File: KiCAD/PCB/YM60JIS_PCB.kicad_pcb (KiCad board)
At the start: 2 copper layers, 285.1 x 94.6 mm, 173 parts, among them J1 TYPE-C-31-M-12, SW1 SW_Push, SW10 SW_Push, SW11 SW_Push, SW12 SW_Push, SW13 SW_Push, SW14 SW_Push, SW15 SW_Push, SW16 SW_Push, SW17 SW_Push, SW18 SW_Push, SW19 SW_Push, SW2 SW_Push, SW20 SW_Push, SW21 SW_Push, SW22 SW_Push, SW23 SW_Push, SW24 SW_Push, SW25 SW_Push, SW26 SW_Push, SW27 SW_Push, SW28 SW_Push, SW29 Space, SW3 SW_Push, SW30 SW_Push, SW31 SW_Push, SW32 SW_Push, SW33 SW_Push, SW34 SW_Push, SW35 SW_Push, SW36 SW_Push, SW37 SW_Push, SW38 SW_Push, SW39 SW_Push, SW4 SW_Push, SW40 SW_Push, SW41 SW_Push, SW42 SW_Push, SW43 SW_Push, SW44 SW_Push, SW45 SW_Push, SW46 SW_Push, SW47 SW_Push, SW48 SW_Push, SW49 SW_Push, SW5 SW_Push, SW50 SW_Push, SW51 SW_Push, SW52 SW_Push, SW53 SW_Push, SW54 SW_Push, SW55 SW_Push, SW56 SW_Push, SW57 SW_Push, SW58 SW_Push, SW59 SW_Push, SW6 SW_Push, SW60 SW_Push, SW61 SW_Push, SW62 SW_Push, SW63 Yen, SW64 Backspace, SW65 ISOEnter, SW66 SW_Push, SW67 SW_Push, SW7 SW_Push, SW8 SW_Push, SW9 SW_Push, U1 XC6206P332MR, U2 SMF05CT1G, U3 RP2040, U4 W25Q16JVUXIQ, Y1 X322512MSB4SI

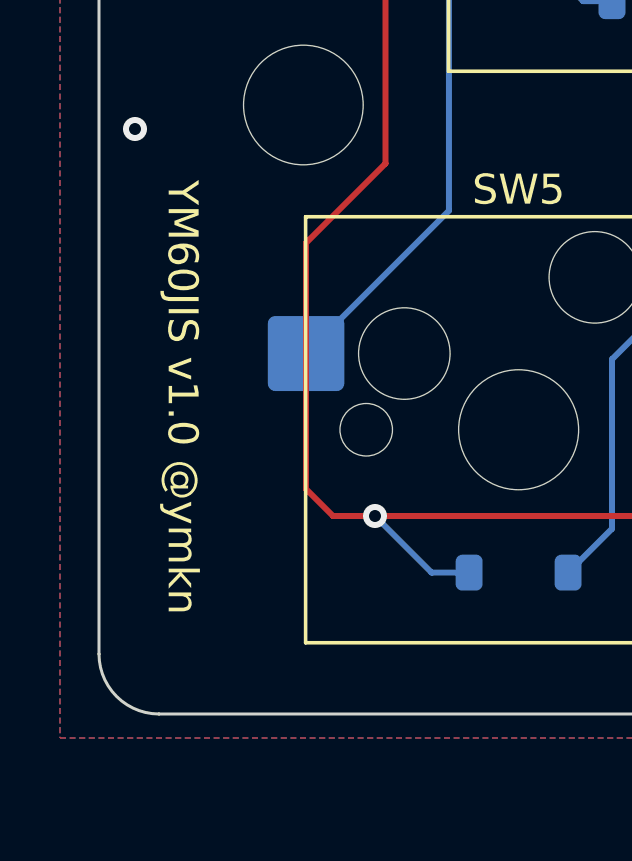
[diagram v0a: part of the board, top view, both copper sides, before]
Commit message: PlateのライブラリパスをPCBと同様にsubmoduleへ変更、穴位置も微調整
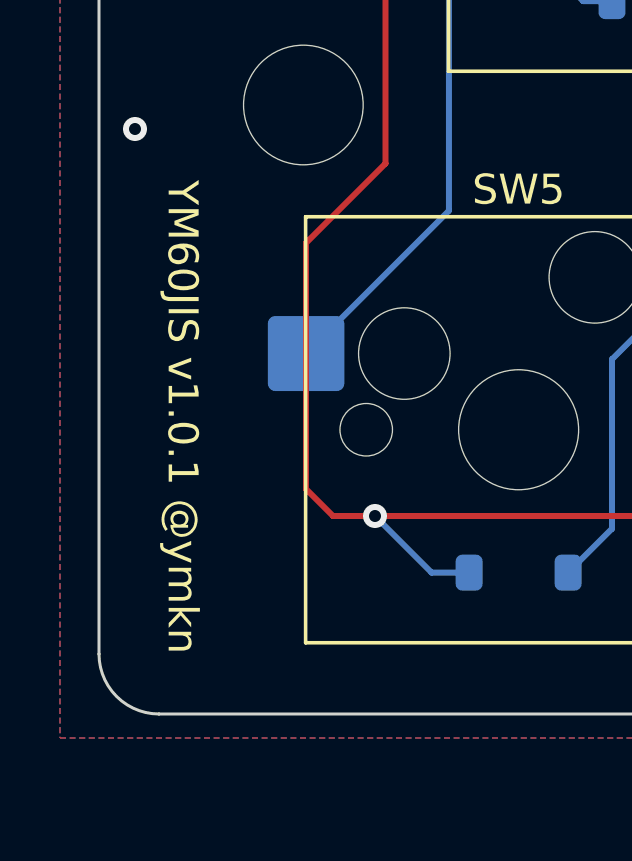
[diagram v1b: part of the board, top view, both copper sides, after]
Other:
- board text added: "YM60JIS v1.0.1 @ymkn"
- board text removed: "YM60JIS v1.0 @ymkn"
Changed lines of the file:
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@@
   (title_block
     (title "YM60JIS PCB")
-    (date "2023-11-11")
-    (rev "v1.0")
+    (date "2024-01-08")
+    (rev "v1.0.1")
     (company "@ymkn")
   )
@@
     (effects (font (size 1 1) (thickness 0.15)) (justify left bottom mirror))
   )
-  (gr_text "YM60JIS v1.0 @ymkn" (at 97.75 125.025 270) (layer "F.SilkS")
+  (gr_text "YM60JIS v1.0.1 @ymkn" (at 97.75 125.025 270) (layer "F.SilkS")
     (effects (font (size 1 1) (thickness 0.15)) (justify left bottom))
   )

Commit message: v1.1およびv1.1.1の追加
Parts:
- REF**: value Stabilizer_Cherry_MX_2.00u -> STAB_MX_ISO; footprint PCM_Mounting_Keyboard_Stabilizer:Stabilizer_Cherry_MX_2.00u -> PCM_marbastlib-mx:STAB_MX_ISO
- REF**: value Stabilizer_Cherry_MX_3.00u -> STAB_MX_2.75u; footprint PCM_Mounting_Keyboard_Stabilizer:Stabilizer_Cherry_MX_3.00u -> PCM_marbastlib-mx:STAB_MX_2.75u
- REF**: value Stabilizer_Cherry_MX_2.00u -> STAB_MX_2u; footprint PCM_Mounting_Keyboard_Stabilizer:Stabilizer_Cherry_MX_2.00u -> PCM_marbastlib-mx:STAB_MX_2u
- REF**: value Stabilizer_Cherry_MX_2.00u -> STAB_MX_3u; footprint PCM_Mounting_Keyboard_Stabilizer:Stabilizer_Cherry_MX_2.00u -> PCM_marbastlib-mx:STAB_MX_3u
- SW1, SW11, SW12, SW13, SW14, SW16, SW17, SW18, SW19, SW21, SW22, SW23, SW24, SW25, SW26, SW27, SW28, SW30, SW31, SW32, SW33, SW34, SW35, SW36, SW37, SW38, SW39, SW40, SW41, SW43, SW44, SW45, SW46, SW48, SW49, SW50, SW51, SW53, SW54, SW55, SW56, SW57, SW58, SW59, SW6, SW60, SW61, SW62, SW63, SW64, SW66, SW67, SW7, SW8, SW9: footprint PCM_Switch_Keyboard_Hotswap_Kailh:SW_Hotswap_Kailh_MX_1.00u -> PCM_marbastlib-mx:SW_MX_HS_CPG151101S11_1u; moved to B.Cu
- SW10, SW15, SW20, SW47, SW52: footprint PCM_Switch_Keyboard_Hotswap_Kailh:SW_Hotswap_Kailh_MX_1.25u -> PCM_marbastlib-mx:SW_MX_HS_CPG151101S11_1.25u; moved to B.Cu
- SW2, SW5: footprint PCM_Switch_Keyboard_Hotswap_Kailh:SW_Hotswap_Kailh_MX_1.50u -> PCM_marbastlib-mx:SW_MX_HS_CPG151101S11_1.5u; moved to B.Cu
- SW29: footprint PCM_Switch_Keyboard_Hotswap_Kailh:SW_Hotswap_Kailh_MX_3.00u -> PCM_marbastlib-mx:SW_MX_HS_CPG151101S11_1u; moved to B.Cu
- SW3: footprint PCM_Switch_Keyboard_Hotswap_Kailh:SW_Hotswap_Kailh_MX_1.75u -> PCM_marbastlib-mx:SW_MX_HS_CPG151101S11_1.75u; moved to B.Cu
- SW4: footprint PCM_Switch_Keyboard_Hotswap_Kailh:SW_Hotswap_Kailh_MX_2.00u -> PCM_marbastlib-mx:SW_MX_HS_CPG151101S11_1u; moved to B.Cu
- SW42: footprint PCM_Switch_Keyboard_Hotswap_Kailh:SW_Hotswap_Kailh_MX_1.25u -> PCM_marbastlib-mx:SW_MX_HS_CPG151101S11_1u; moved to B.Cu
- SW65: footprint PCM_Switch_Keyboard_Hotswap_Kailh:SW_Hotswap_Kailh_MX_ISOEnter -> PCM_marbastlib-mx:SW_MX_HS_CPG151101S11_1u; moved to B.Cu
- turned REF** to 0 degrees
- turned SW1 to 0 degrees
- turned SW10 to 180 degrees
- turned SW11 to 180 degrees
- turned SW12 to 180 degrees
- turned SW13 to 180 degrees
- turned SW14 to 180 degrees
- turned SW15 to 180 degrees
- turned SW16 to 180 degrees
- turned SW17 to 180 degrees
- turned SW18 to 180 degrees
- turned SW19 to 180 degrees
- turned SW2 to 180 degrees
- turned SW20 to 180 degrees
- turned SW21 to 180 degrees
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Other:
- board text added: "YM60JIS v1.1.1 @ymkn"
- board text removed: "YM60JIS v1.0.1 @ymkn"
